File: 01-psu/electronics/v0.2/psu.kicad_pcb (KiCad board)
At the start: 2 copper layers, 250 x 32 mm, 30 parts, among them IC1 ISOLATED_DC-DC_CONV, J1 Barrel_Jack_Switch, J13 Conn_01x03, J2 Conn_02x08_Odd_Even, J3 Conn_02x08_Odd_Even, J4 Conn_02x08_Odd_Even, J5 Conn_02x08_Odd_Even

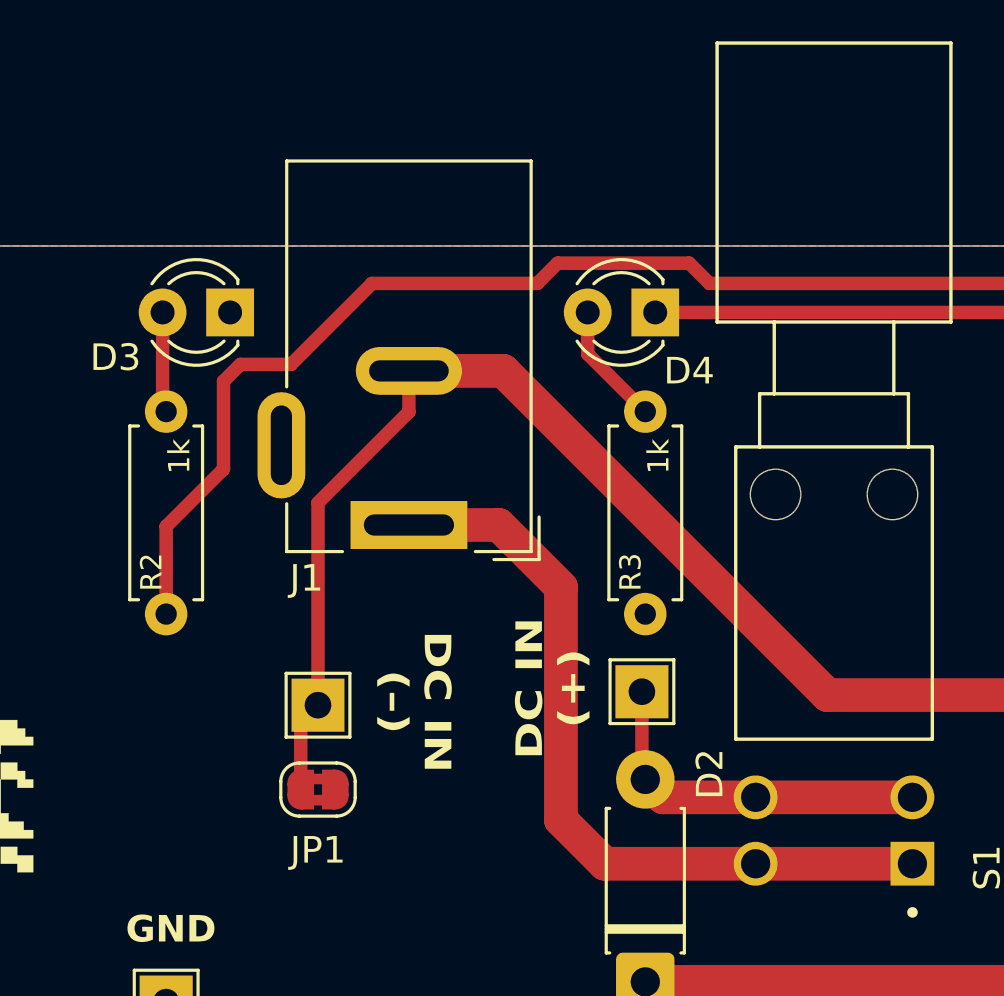
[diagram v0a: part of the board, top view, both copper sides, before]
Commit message: PSU v0.2 and fixed crosstalk on VCA
- added PSU v0.2
- VCA had a crosstalk issue. The input signal got superimposed on the output. The current solution is to move the input voltage divider on the core board as close to the input pin header connection as possible. Additionally, I added the 100k resistor as a THT component to the UI board. Only one of the 100k resistors is needed, but I added both for testing purposes.
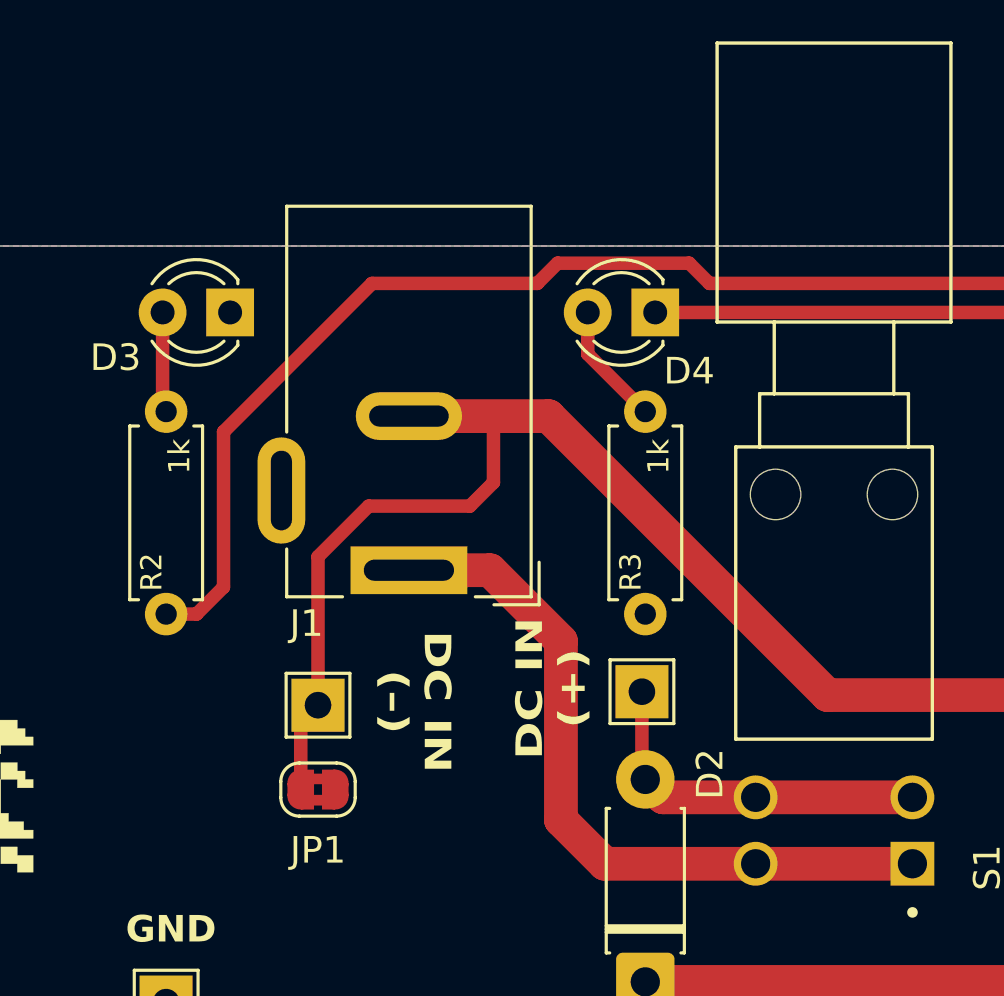
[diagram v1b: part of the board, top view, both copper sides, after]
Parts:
- moved J1 1.70 mm to (56.0, 92.2)
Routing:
- net Net-(J1-Pad1): track 29.4 -> 27.5 mm
- net DC_IN_-: track 62.5 -> 63.6 mm
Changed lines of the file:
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@@
 			(crossoutdnponfab yes)
 			(subtractmaskfromsilk no)
-			(outputformat 1)
+			(outputformat 4)
 			(mirror no)
-			(drillshape 1)
+			(drillshape 2)
 			(scaleselection 1)
-			(outputdirectory "")
+			(outputdirectory "plot/")
 		)
 	)
@@
 	(footprint "Connector_BarrelJack:BarrelJack_Wuerth_6941xx301002"
 		(layer "F.Cu")
-		(at 56 90.5 180)
+		(at 56 92.202 180)
 		(descr "Wuerth electronics barrel jack connector (5.5mm outher diameter, inner diameter 2.05mm or 2.55mm depending on exact order number), See: http://katalog.we-online.de/em/datasheet/6941xx301002.pdf")
 		(tags "connector barrel jack")
@@
 		)
 	)
+	(dimension
+		(type orthogonal)
+		(layer "User.2")
+		(pts
+			(xy 63 80) (xy 63 78.5)
+		)
+		(height -43)
+		(orientation 1)
+		(format
+			(prefix "")
+			(suffix "")
+			(units 3)
+			(units_format 0)
+			(precision 4)
+			(suppress_zeroes yes)
+		)
+		(style
+			(thickness 0.1)
+			(arrow_length 1.27)
+			(text_position_mode 0)
+			(arrow_direction outward)
+			(extension_height 0.58642)
+			(extension_offset 0.5)
+			(keep_text_aligned yes)
+		)
+		(gr_text "1.5"
+			(at 18.85 79.25 90)
+			(layer "User.2")
+			(effects
+				(font
+					(size 1 1)
+					(thickness 0.15)
+				)
+			)
+		)
+	)
+	(segment
+		(start 93.611 96.901)
+		(end 95.2875 98.5775)
+		(width 1.27)
+		(layer "F.Cu")
+		(net 1)
+	)
 	(segment
-		(start 56 84.7)
-		(end 59.554 84.7)
+		(start 56 86.402)
+		(end 61.256 86.402)
 		(width 1.27)
 		(layer "F.Cu")
@@
 	)
 	(segment
-		(start 52.578 97.282)
-		(end 52.578 89.662)
+		(start 59.182 88.9)
+		(end 59.182 86.402)
 		(width 0.508)
 		(layer "F.Cu")
@@
 	)
 	(segment
-		(start 59.554 84.7)
-		(end 71.755 96.901)
-		(width 1.27)
+		(start 52.578 91.694)
+		(end 54.483 89.789)
+		(width 0.508)
 		(layer "F.Cu")
 		(net 1)
 	)
 	(segment
-		(start 93.611 96.901)
-		(end 95.2875 98.5775)
-		(width 1.27)
+		(start 58.293 89.789)
+		(end 59.182 88.9)
+		(width 0.508)
 		(layer "F.Cu")
 		(net 1)
 	)
 	(segment
-		(start 71.755 96.901)
-		(end 93.611 96.901)
-		(width 1.27)
+		(start 52.578 97.282)
+		(end 52.578 91.694)
+		(width 0.508)
+		(layer "F.Cu")
+		(net 1)
+	)
+	(segment
+		(start 54.483 89.789)
+		(end 58.293 89.789)
+		(width 0.508)
 		(layer "F.Cu")
 		(net 1)
@@
 	)
 	(segment
-		(start 56 86.24)
-		(end 56 84.7)
-		(width 0.508)
+		(start 61.256 86.402)
+		(end 71.755 96.901)
+		(width 1.27)
 		(layer "F.Cu")
 		(net 1)
 	)
 	(segment
-		(start 52.578 89.662)
-		(end 56 86.24)
-		(width 0.508)
+		(start 71.755 96.901)
+		(end 93.611 96.901)
+		(width 1.27)
 		(layer "F.Cu")
 		(net 1)
@@
 	)
 	(segment
-		(start 183.261 85.598)
-		(end 149.733 85.598)
-		(width 1.27)
+		(start 49.022 86.995)
+		(end 49.022 92.837)
+		(width 0.508)
 		(layer "F.Cu")
 		(net 4)
 	)
 	(segment
-		(start 49.022 85.09)
-		(end 49.022 88.392)
-		(width 0.508)
+		(start 183.261 85.598)
+		(end 149.733 85.598)
+		(width 1.27)
 		(layer "F.Cu")
 		(net 4)
@@
 	)
 	(segment
+		(start 61.595 80.645)
+		(end 60.833 81.407)
+		(width 0.508)
+		(layer "F.Cu")
+		(net 4)
+	)
+	(segment
 		(start 250.317 87.7745)
 		(end 250.317 85.598)
@@
 	)
 	(segment
-		(start 115.6075 85.8775)
-		(end 100.7365 85.8775)
+		(start 54.61 81.407)
+		(end 49.022 86.995)
 		(width 0.508)
 		(layer "F.Cu")
@@
 	)
 	(segment
-		(start 60.833 81.407)
-		(end 54.61 81.407)
+		(start 100.7365 85.8775)
+		(end 96.266 81.407)
 		(width 0.508)
 		(layer "F.Cu")
@@
 	)
 	(segment
-		(start 264.033 85.598)
-		(end 250.317 85.598)
-		(width 1.27)
+		(start 66.548 80.645)
+		(end 61.595 80.645)
+		(width 0.508)
 		(layer "F.Cu")
 		(net 4)
 	)
 	(segment
-		(start 61.595 80.645)
-		(end 60.833 81.407)
+		(start 115.6075 85.8775)
+		(end 100.7365 85.8775)
 		(width 0.508)
 		(layer "F.Cu")
@@
 	)
 	(segment
-		(start 273.685 89.777)
-		(end 268.212 89.777)
+		(start 264.033 85.598)
+		(end 250.317 85.598)
 		(width 1.27)
 		(layer "F.Cu")
@@
 	)
 	(segment
-		(start 46.863 90.551)
-		(end 46.863 93.853)
-		(width 0.508)
+		(start 273.685 89.777)
+		(end 268.212 89.777)
+		(width 1.27)
 		(layer "F.Cu")
 		(net 4)
@@
 	)
 	(segment
+		(start 48.006 93.853)
+		(end 46.863 93.853)
+		(width 0.508)
+		(layer "F.Cu")
+		(net 4)
+	)
+	(segment
 		(start 115.887 85.598)
 		(end 115.6075 85.8775)
@@
 	)
 	(segment
-		(start 54.61 81.407)
-		(end 51.562 84.455)
-		(width 0.508)
-		(layer "F.Cu")
-		(net 4)
-	)
-	(segment
-		(start 66.548 80.645)
-		(end 61.595 80.645)
-		(width 0.508)
+		(start 250.317 85.598)
+		(end 216.789 85.598)
+		(width 1.27)
 		(layer "F.Cu")
 		(net 4)
 	)
 	(segment
-		(start 100.7365 85.8775)
-		(end 96.266 81.407)
+		(start 67.31 81.407)
+		(end 66.548 80.645)
 		(width 0.508)
 		(layer "F.Cu")
@@
 	)
 	(segment
-		(start 250.317 85.598)
-		(end 216.789 85.598)
-		(width 1.27)
-		(layer "F.Cu")
-		(net 4)
-	)
-	(segment
 		(start 149.733 85.598)
 		(end 115.887 85.598)
@@
 	)
 	(segment
-		(start 183.261 87.7745)
-		(end 183.261 85.598)
-		(width 1.27)
+		(start 60.833 81.407)
+		(end 54.61 81.407)
+		(width 0.508)
 		(layer "F.Cu")
 		(net 4)
 	)
 	(segment
-		(start 149.733 87.7745)
-		(end 149.733 85.598)
+		(start 183.261 87.7745)
+		(end 183.261 85.598)
 		(width 1.27)
 		(layer "F.Cu")
@@
 	)
 	(segment
-		(start 67.31 81.407)
-		(end 66.548 80.645)
+		(start 49.022 92.837)
+		(end 48.006 93.853)
 		(width 0.508)
 		(layer "F.Cu")
@@
 	)
 	(segment
-		(start 49.022 88.392)
-		(end 46.863 90.551)
-		(width 0.508)
+		(start 149.733 87.7745)
+		(end 149.733 85.598)
+		(width 1.27)
 		(layer "F.Cu")
 		(net 4)
@@
 	)
 	(segment
-		(start 51.562 84.455)
-		(end 49.657 84.455)
-		(width 0.508)
-		(layer "F.Cu")
-		(net 4)
-	)
-	(segment
-		(start 49.657 84.455)
-		(end 49.022 85.09)
-		(width 0.508)
-		(layer "F.Cu")
-		(net 4)
-	)
-	(segment
 		(start 97.282 102.489)
 		(end 99.314 100.457)
@@
 	)
 	(segment
-		(start 69.049 103.251)
-		(end 69.05 103.25)
+		(start 59.055 92.202)
+		(end 61.722 94.869)
 		(width 1.27)
 		(layer "F.Cu")
@@
 	)
 	(segment
-		(start 61.722 101.6)
-		(end 63.373 103.251)
+		(start 63.373 103.251)
+		(end 69.049 103.251)
 		(width 1.27)
 		(layer "F.Cu")
@@
 	)
 	(segment
-		(start 69.05 103.25)
-		(end 74.95 103.25)
+		(start 61.722 101.6)
+		(end 63.373 103.251)
 		(width 1.27)
 		(layer "F.Cu")
@@
 	)
 	(segment
-		(start 63.373 103.251)
-		(end 69.049 103.251)
+		(start 69.05 103.25)
+		(end 74.95 103.25)
 		(width 1.27)
 		(layer "F.Cu")
@@
 	)
 	(segment
-		(start 59.385 90.5)
-		(end 61.722 92.837)
+		(start 69.049 103.251)
+		(end 69.05 103.25)
 		(width 1.27)
 		(layer "F.Cu")
@@
 	)
 	(segment
-		(start 61.722 92.837)
-		(end 61.722 101.6)
+		(start 56 92.202)
+		(end 59.055 92.202)
 		(width 1.27)
 		(layer "F.Cu")
@@
 	)
 	(segment
-		(start 56 90.5)
-		(end 59.385 90.5)
+		(start 61.722 94.869)
+		(end 61.722 101.6)
 		(width 1.27)
 		(layer "F.Cu")
